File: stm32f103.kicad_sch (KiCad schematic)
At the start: 47 parts, among them J1 12Vin, J2 SYSTEM_BOOT_JUMP, J3 ADC_PIN, J5 MY_BOOT_JUMP, SW1 RESET, U1 MC33063AD, U2 STM32F103RETx, Y1 8M

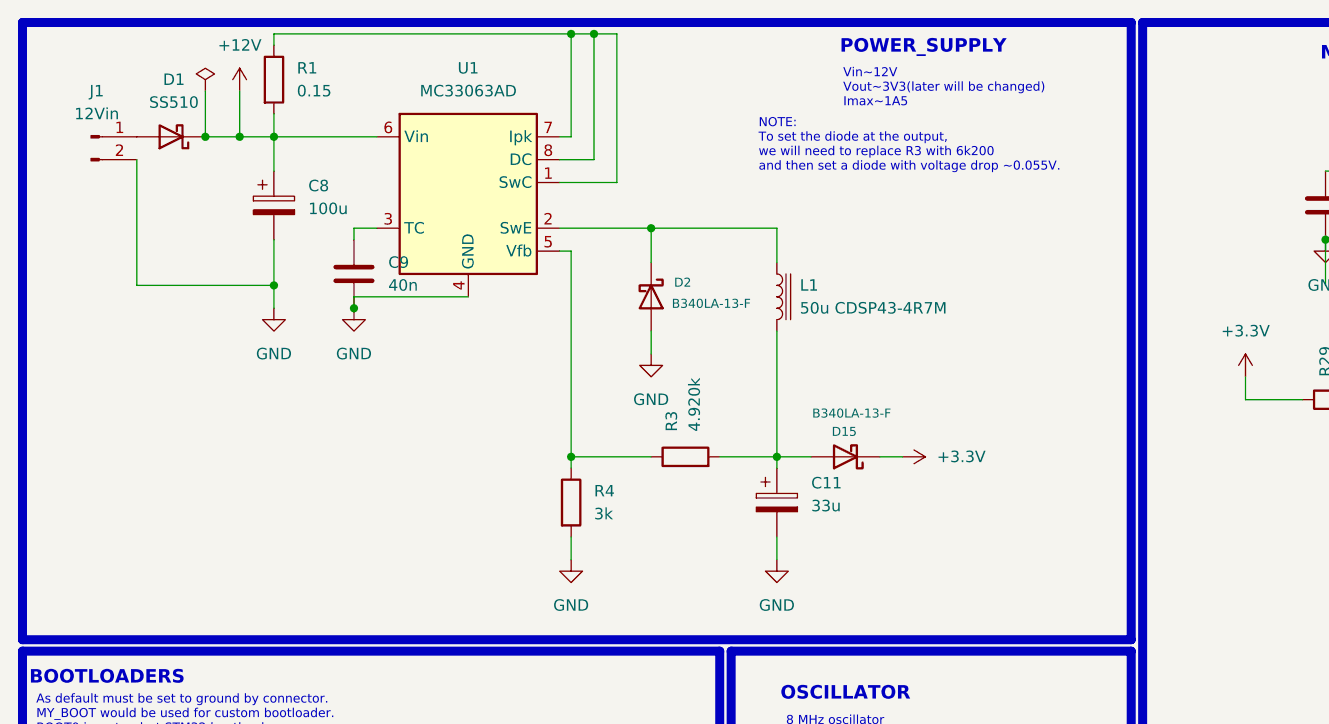
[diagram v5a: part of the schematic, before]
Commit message: Calculations have been made for MC33063 with diode at the output
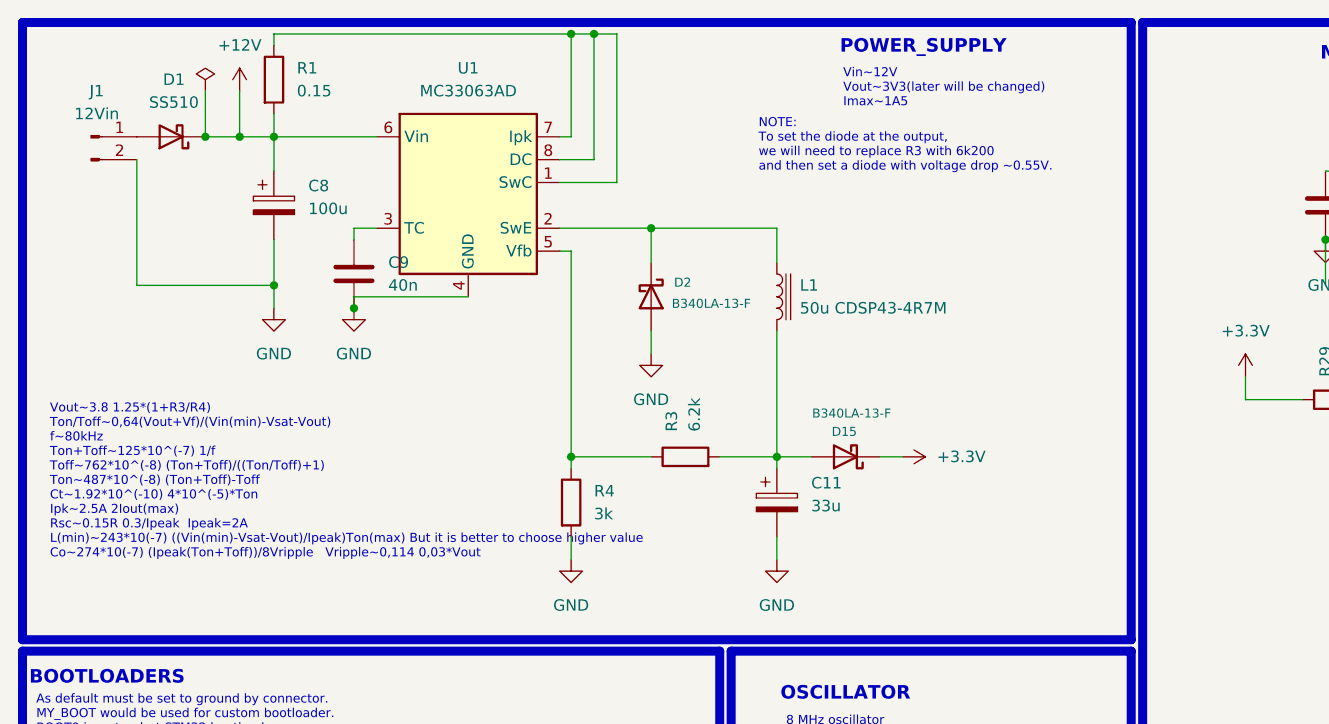
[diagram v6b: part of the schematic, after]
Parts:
- R3: value 4.920k -> 6.2k
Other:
- note added: "NOTE: To set the diode at the output, we will need to replace R3 with 6k200 and then set a diode with voltage drop ~0.55V."
- note added: "Vout~3.8 1.25*(1+R3/R4) Ton/Toff~0,64(Vout+Vf)/(Vin(min)-Vsat-Vout) f~80kHz Ton+Toff~125*10^(-7) 1/f Toff~762*10^(-8) (Ton+Toff)/((Ton/Toff)+1) Ton~487*10^(-8) (Ton+Toff)-Toff Ct~1.92*10^(-10) 4*10^(-5)*Ton Ipk~2.5A 2Iout(max) Rsc~0.15R 0.3/Ipeak Ipeak=2A L(min)~243*10(-7) ((Vin(min)-Vsat-Vout)/Ipeak)Ton(max) But it is better to choose higher value Co~274*10(-7) (Ipeak(Ton+Toff))/8Vripple Vripple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"
- note removed: "NOTE: To set the diode at the output, we will need to replace R3 with 6k200 and then set a diode with voltage drop ~0.055V."
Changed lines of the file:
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@@
 		)
 	)
-	(text "NOTE:\nTo set the diode at the output, \nwe will need to replace R3 with 6k200\nand then set a diode with voltage drop ~0.055V.\n"
+	(text "NOTE:\nTo set the diode at the output, \nwe will need to replace R3 with 6k200\nand then set a diode with voltage drop ~0.55V.\n"
 		(exclude_from_sim no)
 		(at 94.488 26.416 0)
@@
 		)
 	)
+	(text "Vout~3.8 1.25*(1+R3/R4)\nTon/Toff~0,64(Vout+Vf)/(Vin(min)-Vsat-Vout)\nf~80kHz\nTon+Toff~125*10^(-7) 1/f\nToff~762*10^(-8) (Ton+Toff)/((Ton/Toff)+1)\nTon~487*10^(-8) (Ton+Toff)-Toff\nCt~1.92*10^(-10) 4*10^(-5)*Ton\nIpk~2.5A 2Iout(max)\nRsc~0.15R 0.3/Ipeak  Ipeak=2A\nL(min)~243*10(-7) ((Vin(min)-Vsat-Vout)/Ipeak)Ton(max) But it is better to choose higher value\nCo~274*10(-7) (Ipeak(Ton+Toff))/8Vripple   Vripple~0,114 0,03*Vout\n"
+		(exclude_from_sim no)
+		(at 15.748 63.754 0)
+		(effects
+			(font
+				(size 1 1)
+				(thickness 0.125)
+				(color 0 0 0 1)
+			)
+			(justify left)
+		)
+	)
 	(text "OSCILLATOR"
 		(exclude_from_sim no)
@@
 			)
 		)
-		(property "Value" "4.920k"
+		(property "Value" "6.2k"
 			(at 87.376 58.166 0)
 			(effects

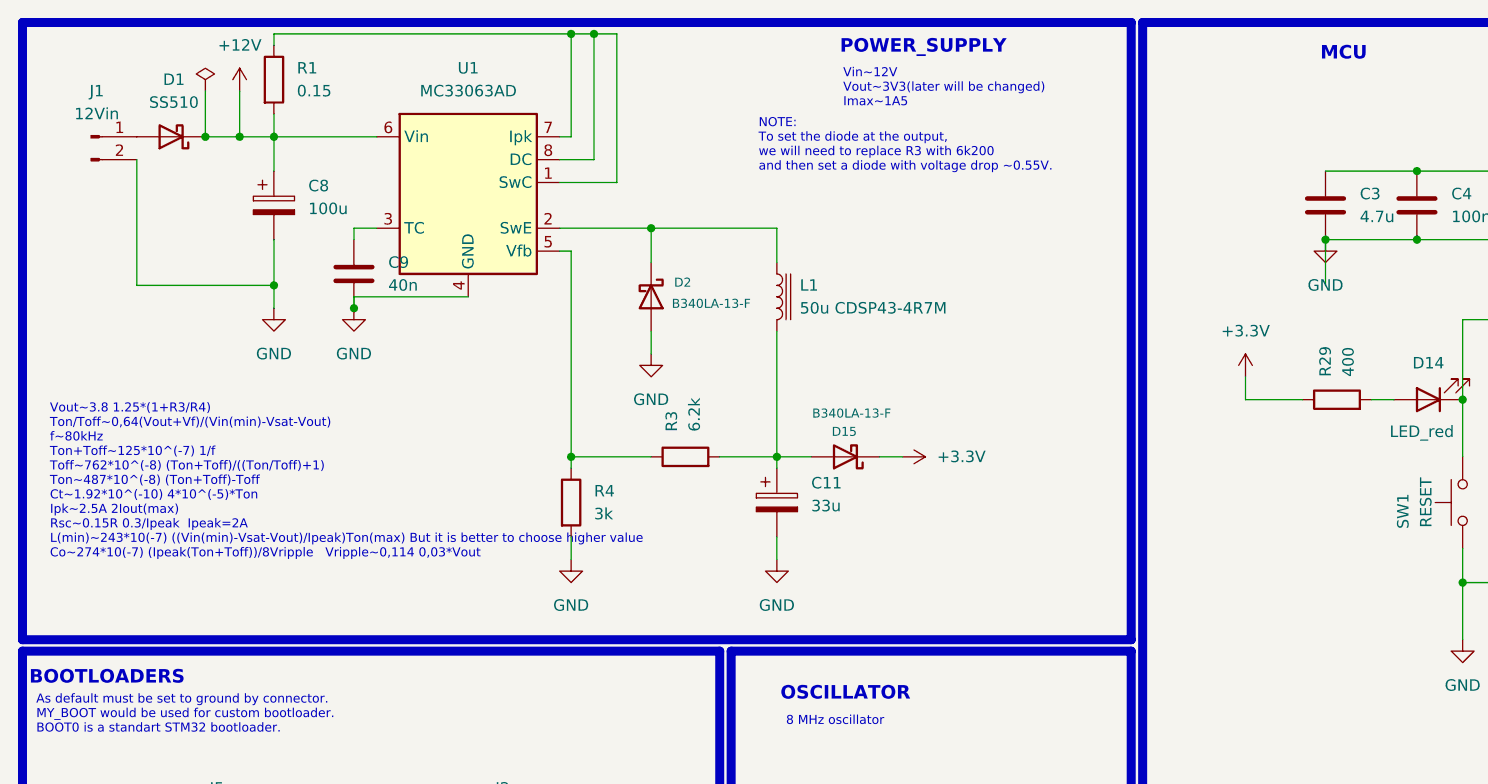
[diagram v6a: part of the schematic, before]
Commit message: CH340N has been added. Previous version was wrong. Pin V3 was wrong placed and was connected to GND
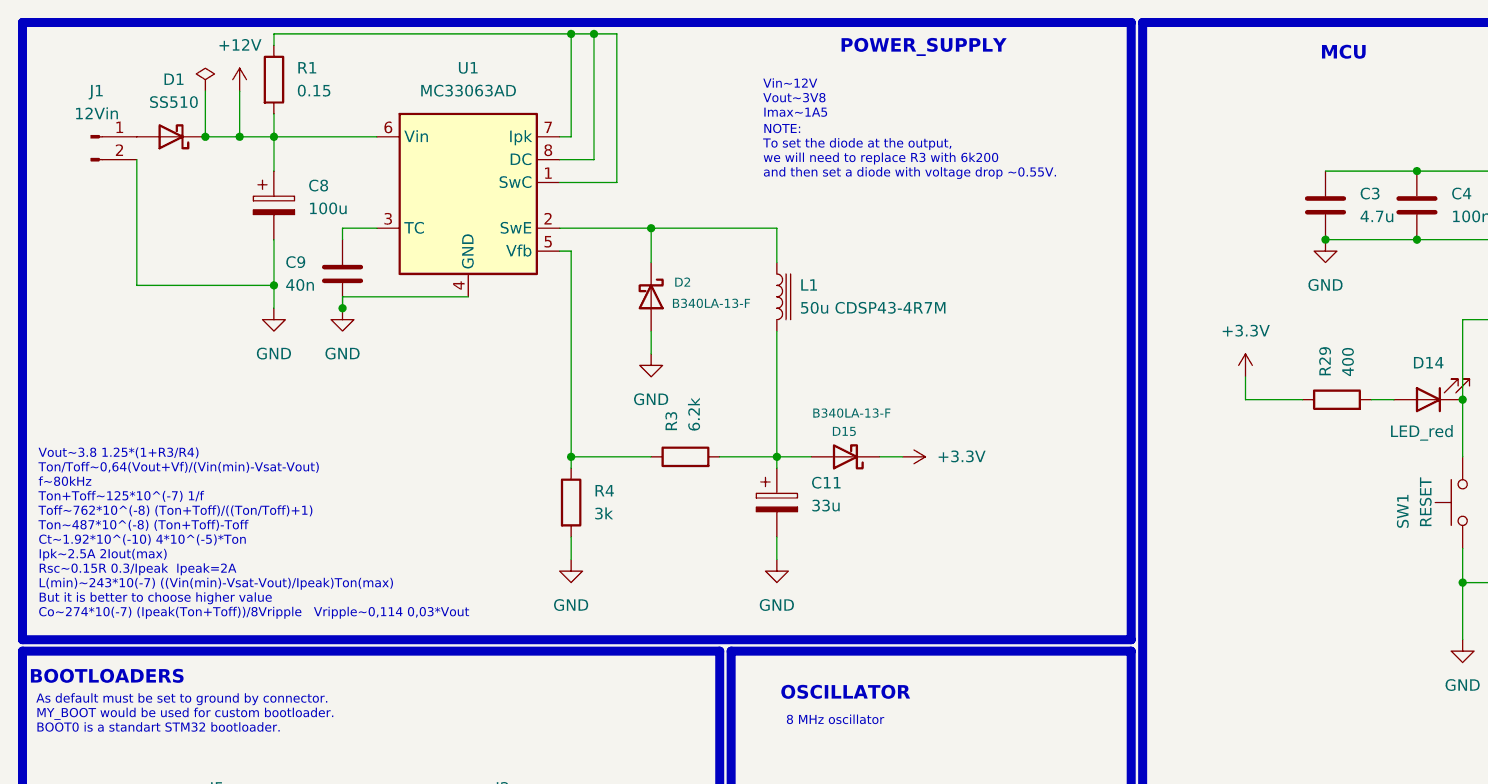
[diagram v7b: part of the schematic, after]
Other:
- note added: "Vin~12V Vout~3V8 Imax~1A5"
- note removed: "Vin~12V Vout~3V3(later will be changed) Imax~1A5"
- company: (none) -> HOMEMADE
- title: (none) -> ProgrammLockControl(MCU and power)
- moved on the sheet: C9
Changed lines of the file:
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@@
 	(generator_version "9.0")
 	(paper "A4")
+	(title_block
+		(title "ProgrammLockControl(MCU and power)")
+		(date "2025-11-25")
+		(rev "V2.0")
+		(company "HOMEMADE")
+	)
 	(rectangle
 		(start 12.7 82.55)
@@
 		)
 	)
-	(text "Vin~12V\nVout~3V3(later will be changed)\nImax~1A5"
+	(text "Vin~12V\nVout~3V8\nImax~1A5"
 		(exclude_from_sim no)
-		(at 103.886 20.066 0)
+		(at 94.996 21.336 0)
 		(effects
 			(font
@@
 	(text "NOTE:\nTo set the diode at the output, \nwe will need to replace R3 with 6k200\nand then set a diode with voltage drop ~0.55V.\n"
 		(exclude_from_sim no)
-		(at 94.488 26.416 0)
+		(at 94.996 27.178 0)
 		(effects
 			(font
@@
 		)
 	)
-	(text "Vout~3.8 1.25*(1+R3/R4)\nTon/Toff~0,64(Vout+Vf)/(Vin(min)-Vsat-Vout)\nf~80kHz\nTon+Toff~125*10^(-7) 1/f\nToff~762*10^(-8) (Ton+Toff)/((Ton/Toff)+1)\nTon~487*10^(-8) (Ton+Toff)-Toff\nCt~1.92*10^(-10) 4*10^(-5)*Ton\nIpk~2.5A 2Iout(max)\nRsc~0.15R 0.3/Ipeak  Ipeak=2A\nL(min)~243*10(-7) ((Vin(min)-Vsat-Vout)/Ipeak)Ton(max) But it is better to choose higher value\nCo~274*10(-7) (Ipeak(Ton+Toff))/8Vripple   Vripple~0,114 0,03*Vout\n"
+	(text "Vout~3.8 1.25*(1+R3/R4)\nTon/Toff~0,64(Vout+Vf)/(Vin(min)-Vsat-Vout)\nf~80kHz\nTon+Toff~125*10^(-7) 1/f\nToff~762*10^(-8) (Ton+Toff)/((Ton/Toff)+1)\nTon~487*10^(-8) (Ton+Toff)-Toff\nCt~1.92*10^(-10) 4*10^(-5)*Ton\nIpk~2.5A 2Iout(max)\nRsc~0.15R 0.3/Ipeak  Ipeak=2A\nL(min)~243*10(-7) ((Vin(min)-Vsat-Vout)/Ipeak)Ton(max) \nBut it is better to choose higher value\nCo~274*10(-7) (Ipeak(Ton+Toff))/8Vripple   Vripple~0,114 0,03*Vout\n"
 		(exclude_from_sim no)
-		(at 15.748 63.754 0)
+		(at 14.478 69.596 0)
 		(effects
 			(font
@@
 	)
 	(junction
-		(at 49.53 44.45)
+		(at 48.26 44.45)
 		(diameter 0)
 		(color 0 0 0 0)
@@
 	(wire
 		(pts
-			(xy 62.23 43.18) (xy 49.53 43.18)
+			(xy 48.26 43.18) (xy 62.23 43.18)
 		)
 		(stroke
@@
 	(wire
 		(pts
-			(xy 49.53 35.56) (xy 52.07 35.56)
+			(xy 48.26 35.56) (xy 52.07 35.56)
 		)
 		(stroke
@@
 	(wire
 		(pts
-			(xy 49.53 36.83) (xy 49.53 35.56)
+			(xy 48.26 36.83) (xy 48.26 35.56)
 		)
 		(stroke
@@
 	(wire
 		(pts
-			(xy 157.48 36.83) (xy 157.48 41.91)
-		)
-		(stroke
-			(width 0)
-			(type default)
-		)
-	)
-	(wire
-		(pts
 			(xy 73.66 60.96) (xy 73.66 38.1)
 		)
@@
 	(wire
 		(pts
-			(xy 49.53 43.18) (xy 49.53 44.45)
+			(xy 48.26 43.18) (xy 48.26 44.45)
 		)
 		(stroke
@@
 	(symbol
 		(lib_id "Device:C")
-		(at 49.53 40.64 0)
+		(at 48.26 40.64 0)
 		(unit 1)
 		(exclude_from_sim no)
@@
 		(on_board yes)
 		(dnp no)
-		(fields_autoplaced yes)
 		(property "Reference" "C9"
-			(at 53.34 39.3699 0)
+			(at 41.91 39.37 0)
 			(effects
 				(font
@@
 		)
 		(property "Value" "40n"
-			(at 53.34 41.9099 0)
+			(at 41.91 41.91 0)
 			(effects
 				(font
@@
 		)
 		(property "Footprint" "Capacitor_SMD:C_1812_4532Metric_Pad1.57x3.40mm_HandSolder"
-			(at 50.4952 44.45 0)
+			(at 49.2252 44.45 0)
 			(effects
 				(font
@@
 		)
 		(property "Datasheet" "~"
-			(at 49.53 40.64 0)
+			(at 48.26 40.64 0)
 			(effects
 				(font
@@
 		)
 		(property "Description" "Unpolarized capacitor"
-			(at 49.53 40.64 0)
+			(at 48.26 40.64 0)
 			(effects
 				(font
@@
 	(symbol
 		(lib_id "power:GND")
-		(at 49.53 44.45 0)
+		(at 48.26 44.45 0)
 		(unit 1)
 		(exclude_from_sim no)
@@
 		(fields_autoplaced yes)
 		(property "Reference" "#PWR07"
-			(at 49.53 50.8 0)
+			(at 48.26 50.8 0)
 			(effects
 				(font
@@
 		)
 		(property "Value" "GND"
-			(at 49.53 49.53 0)
+			(at 48.26 49.53 0)
 			(effects
 				(font
@@
 		)
 		(property "Footprint" ""
-			(at 49.53 44.45 0)
+			(at 48.26 44.45 0)
 			(effects
 				(font
@@
 		)
 		(property "Datasheet" ""
-			(at 49.53 44.45 0)
+			(at 48.26 44.45 0)
 			(effects
 				(font
@@
 		)
 		(property "Description" "Power symbol creates a global label with name \"GND\" , ground"
-			(at 49.53 44.45 0)
+			(at 48.26 44.45 0)
 			(effects
 				(font

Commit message: Shottky diod has been added to provide protection for AMS1117-3.3
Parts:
- C9: value 40n -> 1n
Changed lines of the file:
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@@
 			)
 		)
-		(property "Value" "40n"
+		(property "Value" "1n"
 			(at 41.91 41.91 0)
 			(effects
